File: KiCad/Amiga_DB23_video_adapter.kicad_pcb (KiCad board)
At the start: 2 copper layers, 34.6 x 20 mm, 18 parts, among them J1 DB23_Female, J2 Conn_02x06_Odd_Even, J3 Conn_01x03, SW1 SW_SPDT, U1 74HCT2G17, U2 74HCT2G14, X1 K50-HC0CSE28.6363MR

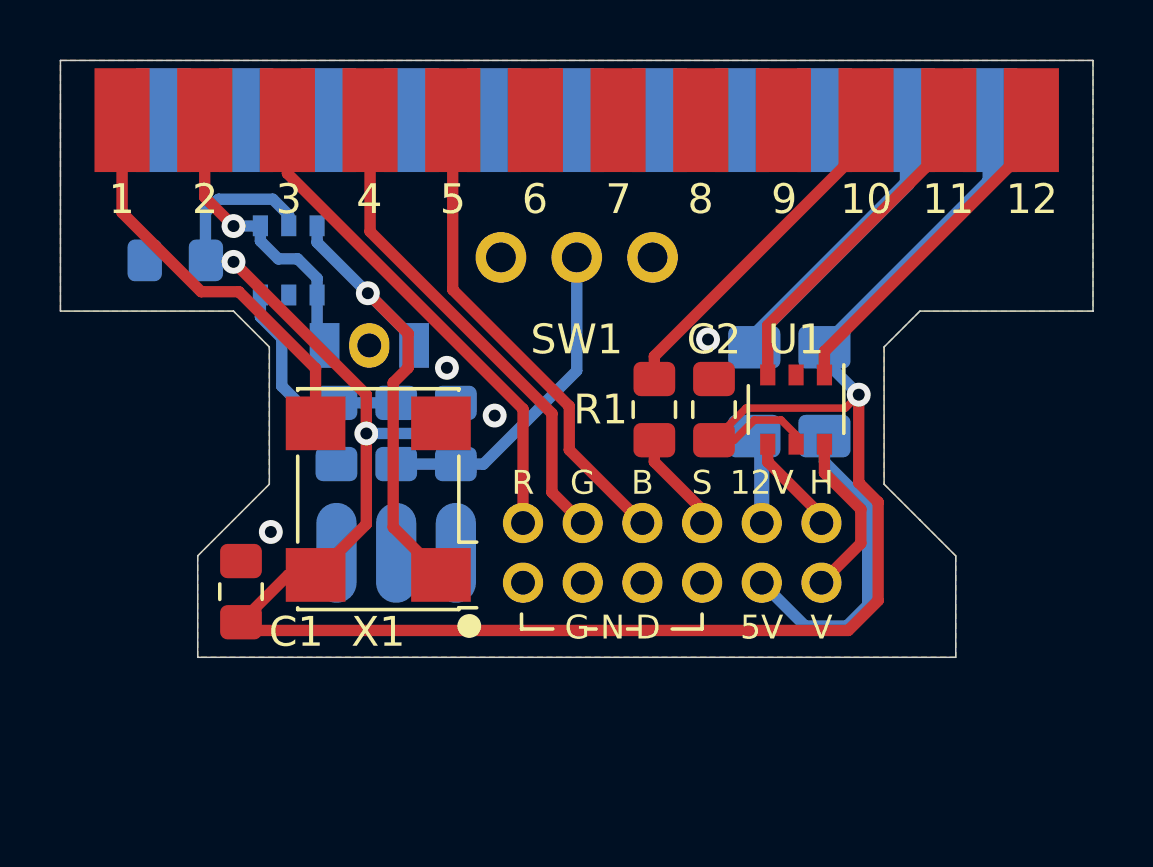
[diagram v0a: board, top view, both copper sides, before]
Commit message: Add new design based on a THS7374IPWR, 28M oscillator circuit, remove SolderJumper, complete re-design and re-route
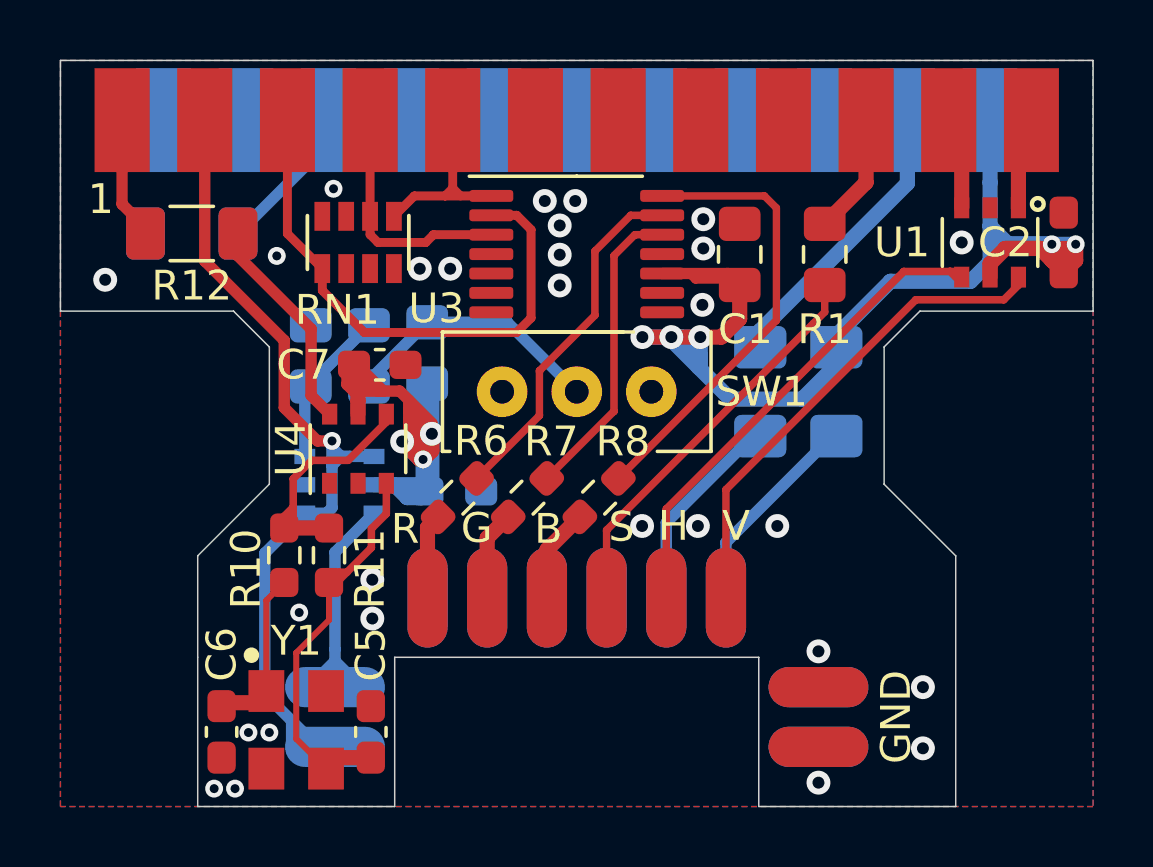
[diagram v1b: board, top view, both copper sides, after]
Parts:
- removed JP1: SolderJumper_3_Open, Jumper:SolderJumper-3_P1.3mm_Open_Pad1.0x1.5mm_NumberLabels
- removed REF**: OSHW-Logo_5.7x6mm_SilkScreen, Symbol:OSHW-Logo_5.7x6mm_SilkScreen
- removed X1: K50-HC0CSE28.6363MR, Oscillator:Oscillator_SMD_SeikoEpson_SG8002CA-4Pin_7.0x5.0mm
- added C5: 32 pF, Capacitor_SMD:C_0603_1608Metric_Pad1.08x0.95mm_HandSolder, F.Cu at (99.6, 72.5)
- added C6: 32 pF, Capacitor_SMD:C_0603_1608Metric_Pad1.08x0.95mm_HandSolder, F.Cu at (94.6, 72.5)
- added C7: 0.1uF, Capacitor_SMD:C_0603_1608Metric_Pad1.08x0.95mm_HandSolder, F.Cu at (99.9, 60.2)
- added J4: Conn_01x02, Connector_PinHeader_2.00mm:PinHeader_1x02_P2.00mm_Vertical, F.Cu at (114.6, 71.0)
- added J5: Conn_01x02, Connector_PinHeader_2.00mm:PinHeader_1x02_P2.00mm_Vertical, B.Cu at (114.6, 71.0)
- added J6: Conn_01x02, Connector_PinHeader_2.00mm:PinHeader_1x02_P2.00mm_Vertical, B.Cu at (98.4, 71.0)
- added R10: 1k, Resistor_SMD:R_0603_1608Metric_Pad0.98x0.95mm_HandSolder, F.Cu at (96.7, 66.6)
- added R11: 2.2M, Resistor_SMD:R_0603_1608Metric_Pad0.98x0.95mm_HandSolder, F.Cu at (98.2, 66.6)
- added R12: 150, Resistor_SMD:R_1206_3216Metric_Pad1.30x1.75mm_HandSolder, F.Cu at (93.6, 55.8)
- added R6: 75, Resistor_SMD:R_0603_1608Metric_Pad0.98x0.95mm_HandSolder, F.Cu at (102.5, 64.7)
- added R7: 75, Resistor_SMD:R_0603_1608Metric_Pad0.98x0.95mm_HandSolder, F.Cu at (104.8, 64.7)
- added R8: 75, Resistor_SMD:R_0603_1608Metric_Pad0.98x0.95mm_HandSolder, F.Cu at (107.2, 64.7)
- added R9: 100, Resistor_SMD:R_1206_3216Metric_Pad1.30x1.75mm_HandSolder, B.Cu at (93.6, 55.8)
- added RN1: R_Pack04, Amiga_DB23_video_adapter:RESCAF80P320X160X60-8N, F.Cu at (99.2, 56.1)
- added U3: THS7374IPWR, Package_SO:TSSOP-14_4.4x5mm_P0.65mm, F.Cu at (106.5, 56.5)
- added U4: 74LVC1GX04, Package_SO:TSOP-6_1.65x3.05mm_P0.95mm, F.Cu at (99.2, 63.0)
- added Y1: CL=16pF, Crystal:Crystal_SMD_SeikoEpson_FA238-4Pin_3.2x2.5mm, F.Cu at (97.1, 72.4)
- C2, C4: footprint Capacitor_SMD:C_0805_2012Metric_Pad1.15x1.40mm_HandSolder -> Capacitor_SMD:C_0603_1608Metric_Pad1.08x0.95mm_HandSolder
- J2: value Conn_02x06_Odd_Even -> Conn_01x06; footprint Connector_PinHeader_2.00mm:PinHeader_2x06_P2.00mm_Vertical -> Connector_PinHeader_2.00mm:PinHeader_1x06_P2.00mm_Vertical
- J3: value Conn_01x03 -> Conn_01x06; footprint Connector_PinHeader_2.00mm:PinHeader_1x03_P2.00mm_Vertical -> Connector_PinHeader_2.00mm:PinHeader_1x06_P2.00mm_Vertical
- moved C1 20.2 mm to (112.0, 56.5)
- moved C2 13.0 mm to (122.8, 56.1)
- moved C4 12.1 mm to (102.4, 64.4), turned to 180 degrees
- moved U1 8.58 mm to (120.3, 56.1)
- moved J3 8.43 mm to (106.5, 68.0)
- moved R1 7.72 mm to (114.8, 56.5)
- moved U2 7.71 mm to (98.5, 64.2), turned to 0 degrees
- moved SW1 5.17 mm to (106.5, 61.1)
- moved R4 2.87 mm to (101.5, 59.8), turned to 90 degrees
- moved R5 2.75 mm to (99.5, 59.9)
- moved C3 2.74 mm to (97.6, 59.9), turned to 90 degrees
- moved J2 1.87 mm to (106.5, 68.0), turned to 270 degrees
- moved R2 0.40 mm to (115.2, 61.1)
- moved R3 0.20 mm to (112.7, 61.1)
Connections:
- J1 pad 3: RED -> AMIGA_R
- J1 pad 4: GREEN -> AMIGA_G
- J1 pad 5: BLUE -> AMIGA_B
- J2 pad 1: GND -> V
- J2 pad 2: RED -> H
- J2 pad 3: GND -> S
- J2 pad 4: GREEN -> /B
- J2 pad 5: GND -> /G
- J2 pad 6: BLUE -> /R
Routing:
- net XCLKEN: track 10.1 -> 30.6 mm
- net AMIGA_R: track 0.00 -> 18.5 mm
- net Net-(C5-Pad1): track 0.00 -> 13.8 mm
- net H: track 3.39 -> 16.7 mm
- net V: track 5.69 -> 16.5 mm
- net S: track 3.44 -> 13.5 mm
- net VCC: track 75.8 -> 85.6 mm, vias 3 -> 8
- net XCLK: track 13.6 -> 4.13 mm
- net OE: track 16.2 -> 7.01 mm, vias 1 -> 0
- net VSYNC: track 11.4 -> 3.12 mm
- net Net-(R10-Pad1): track 0.00 -> 8.27 mm
- net AMIGA_G: track 0.00 -> 8.11 mm
- net HSYNC: track 11.1 -> 3.12 mm
- net Net-(R12-Pad2): track 0.00 -> 7.32 mm
- net /CSYNC: track 11.6 -> 4.41 mm
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- added copper zone on GND, net GND
- added copper zone on VCC, net VCC
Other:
- board size 34.6 x 20 mm -> 34.6 x 25 mm
- copper layers 2 -> 4
- rule pad_to_mask_clearance: 0.051 -> 0
- rule via_min_size: 0.4 -> 0.6
- board text added: "GND"
- board text added: "XCLKEN"
- board text removed: "10"
- board text removed: "11"
- board text removed: "12"
- board text removed: "14"
- board text removed: "15"
- board text removed: "16"
- board text removed: "17"
- board text removed: "18"
- board text removed: "19"
- board text removed: "2"
- board text removed: "20"
- board text removed: "21"
- board text removed: "22"
- board text removed: "3"
- board text removed: "4"
- board text removed: "5"
- board text removed: "6"
- board text removed: "7"
- board text removed: "8"
- board text removed: "9"
- board text removed: "G N D"

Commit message: Improve GND-stitching and fix silkscreen text and add new revision identifier
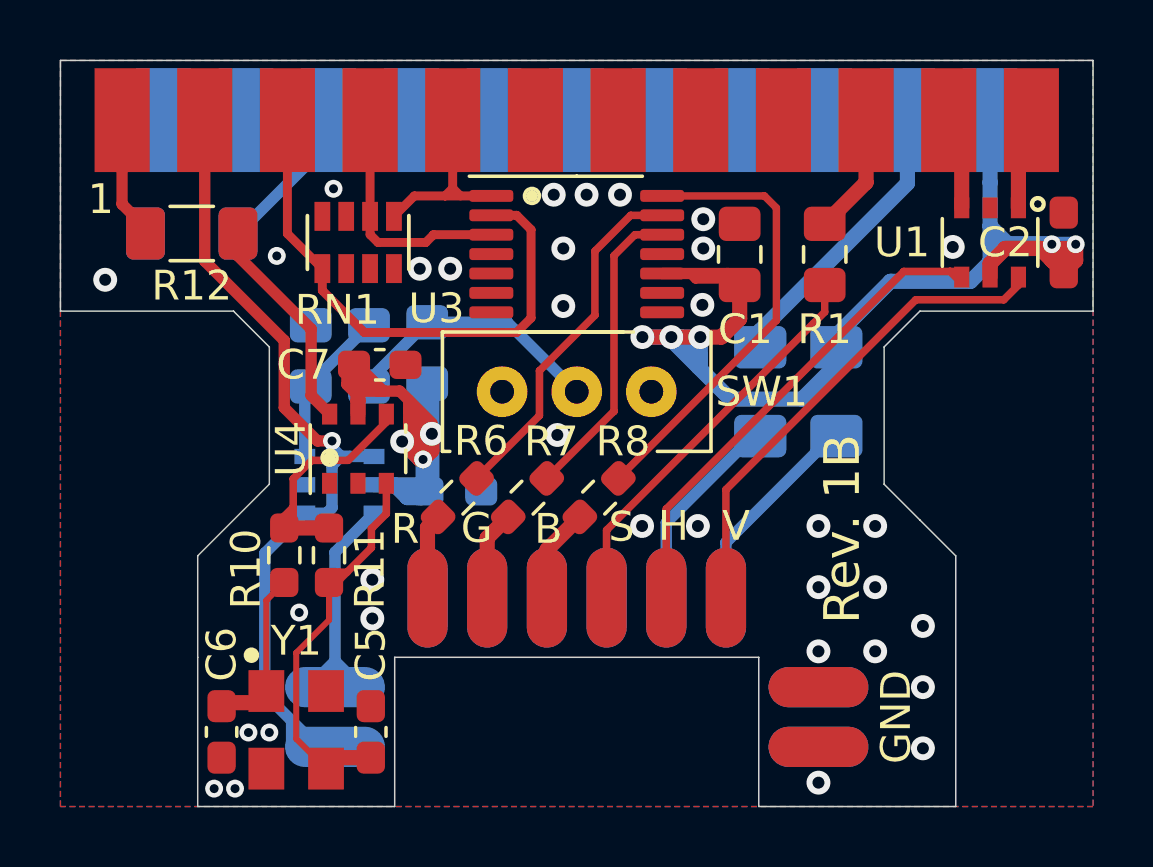
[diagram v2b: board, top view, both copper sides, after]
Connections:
- J1 pad 2: XCLKEN -> XCLKEN_n
- J6 pad 1: OE -> XCLKEN
- J6 pad 2: XCLKEN -> XCLKEN_n
- U2 pad 1: XCLKEN -> XCLKEN_n
- U2 pad 4: XCLKEN -> XCLKEN_n
- U2 pad 6: OE -> XCLKEN
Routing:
- net XCLKEN_n: track 0.00 -> 30.6 mm, vias 0 -> 1
- net XCLKEN: track 30.6 -> 7.01 mm, vias 1 -> 0
- net OE: track 7.01 -> 0.00 mm
- net GND: vias 28 -> 34
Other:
- board text added: "Amiga DB23 Video Adapter Design by J.Bilander"
- board text added: "G N D"
- board text added: "Rev. 1B"

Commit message: Swap references C2,C3. Swap references C5,C7. Swap references R1,R9. Swap references R4,R12
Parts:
- renumbered C3 to C2, C2 to C3, C7 to C5, C5 to C7, R9 to R1, R4 to R12, R12 to R4, R1 to R9

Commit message: Swap references R5,R9. Swap references R10,R12
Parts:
- removed the R12 at (101.5, 59.8)
- added R10: 10k, Resistor_SMD:R_0805_2012Metric_Pad1.15x1.40mm_HandSolder, B.Cu at (101.5, 59.8)
- renumbered R10 to R12, R9 to R5, R5 to R9

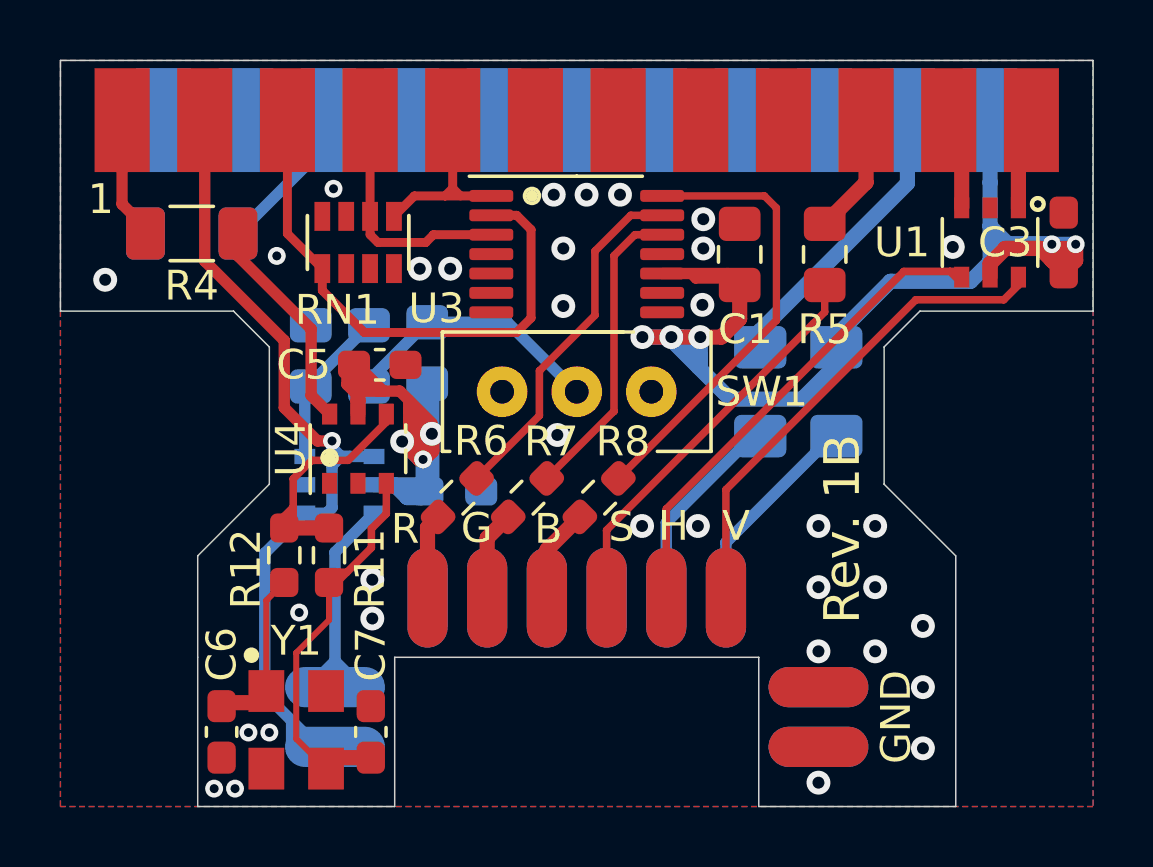
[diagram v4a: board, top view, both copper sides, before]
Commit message: Swap references R11,R12 and fix positioning of R10
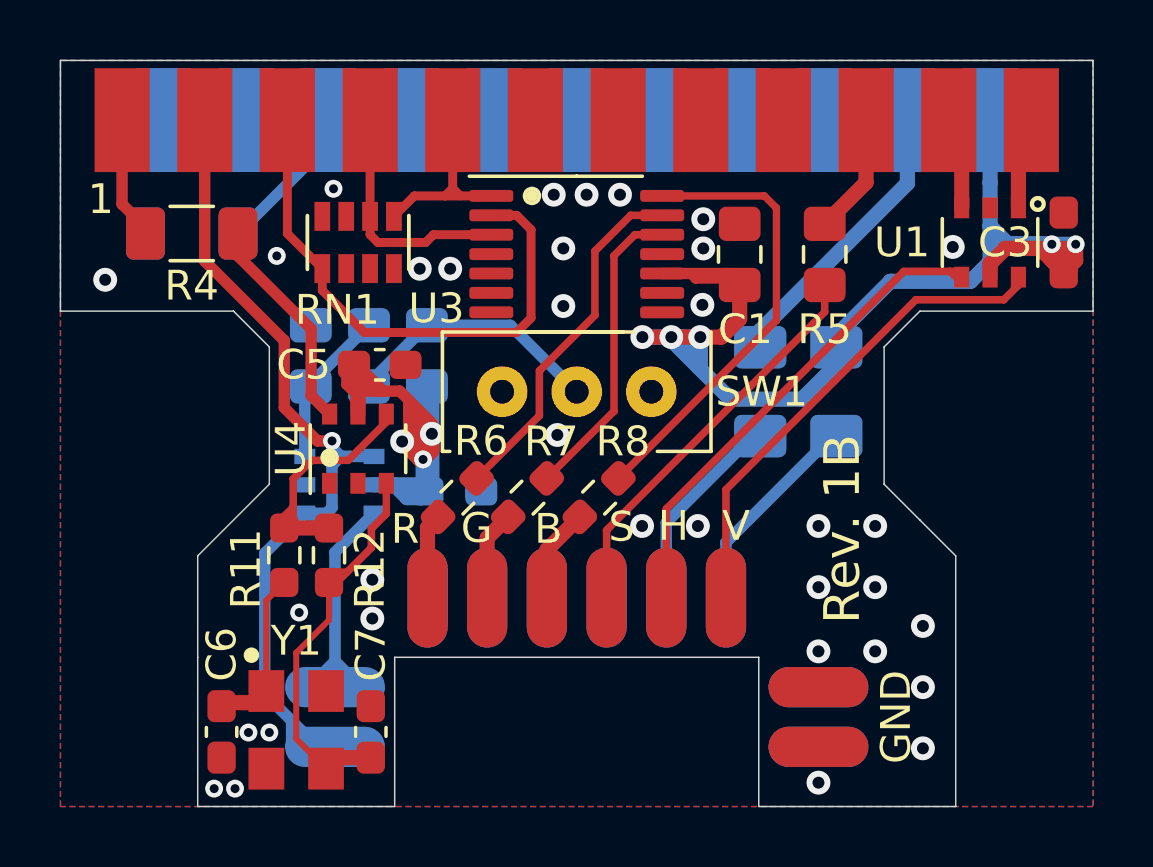
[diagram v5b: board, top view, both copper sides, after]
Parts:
- moved R10 0.10 mm to (101.5, 59.9)
- renumbered R12 to R11, R11 to R12
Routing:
- net VCC: track 85.6 -> 84.3 mm
